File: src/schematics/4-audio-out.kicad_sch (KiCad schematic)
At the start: 7 parts

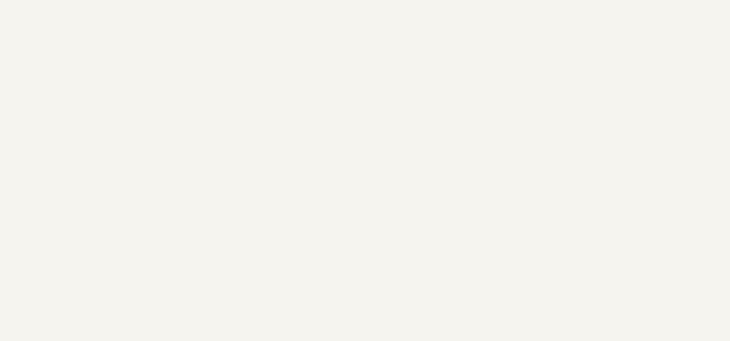
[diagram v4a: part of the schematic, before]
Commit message: Started to draw the MSF receiver based on the simulation learnings.
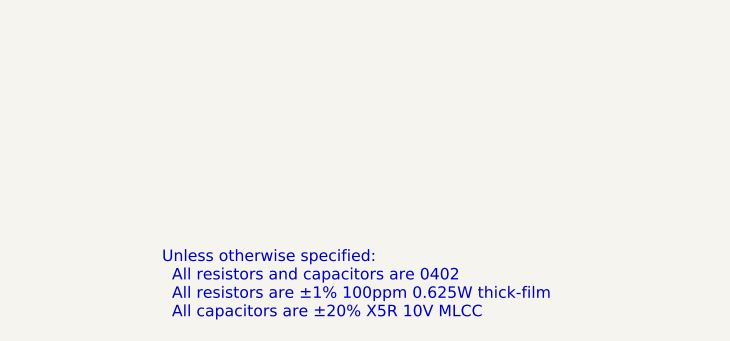
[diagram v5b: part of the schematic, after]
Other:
- note added: "Unless otherwise specified: All resistors and capacitors are 0402 All resistors are ±1% 100ppm 0.625W thick-film All capacitors are ±20% X5R 10V MLCC"
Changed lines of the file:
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@@
+    (effects (font (size 1.27 1.27)) (justify left bottom))
+  )
+  (text "Unless otherwise specified:\n  All resistors and capacitors are 0402\n  All resistors are ±1% 100ppm 0.625W thick-film\n  All capacitors are ±20% X5R 10V MLCC "
+    (at 301.244 261.62 0)
     (effects (font (size 1.27 1.27)) (justify left bottom))
   )

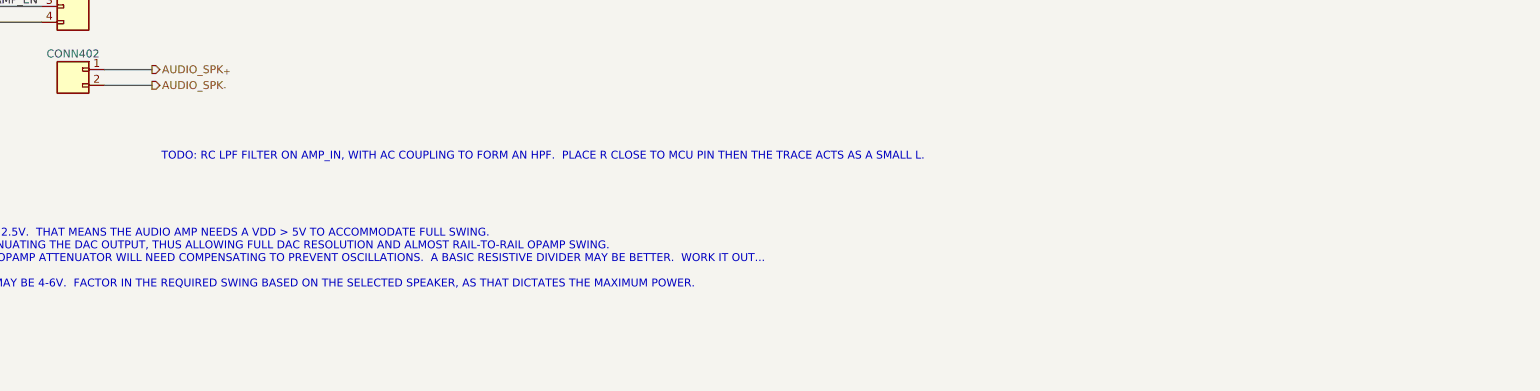
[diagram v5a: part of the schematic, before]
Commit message: Further elaboration of the MSF front-end.
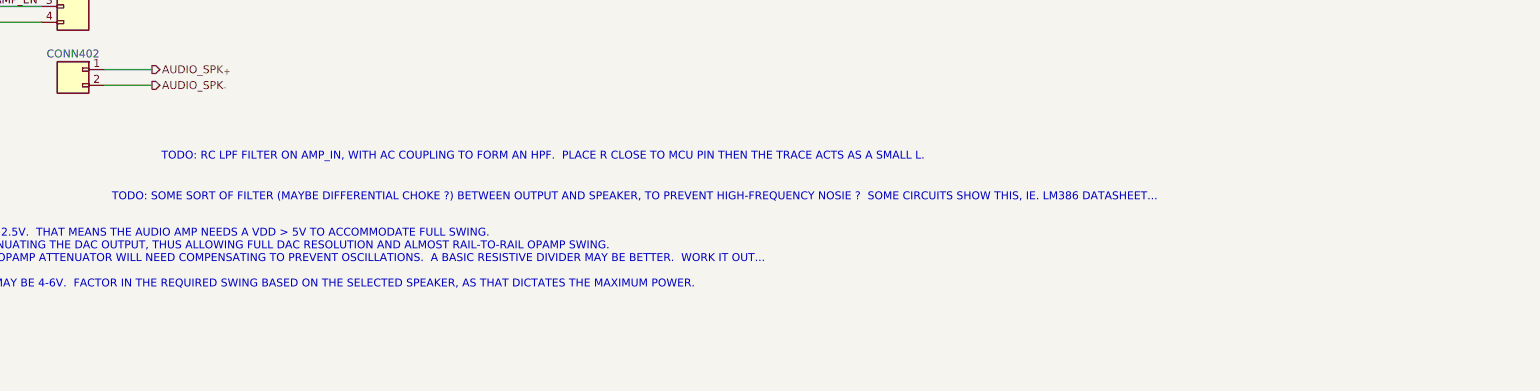
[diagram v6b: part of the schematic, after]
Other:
- note added: "TODO: SOME SORT OF FILTER (MAYBE DIFFERENTIAL CHOKE ?) BETWEEN OUTPUT AND SPEAKER, TO PREVENT HIGH-FREQUENCY NOSIE ? SOME CIRCUITS SHOW THIS, IE. LM386 DATASHEET..."
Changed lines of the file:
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@@
+    (effects (font (size 1.27 1.27)) (justify left bottom))
+  )
+  (text "TODO: SOME SORT OF FILTER (MAYBE DIFFERENTIAL CHOKE ?) BETWEEN OUTPUT AND SPEAKER, TO PREVENT HIGH-FREQUENCY NOSIE ?  SOME CIRCUITS SHOW THIS, IE. LM386 DATASHEET..."
+    (at 107.8471 96.2072 0)
     (effects (font (size 1.27 1.27)) (justify left bottom))
   )

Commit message: Started to elaborate the audio output circuitry.
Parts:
- removed C67: 4.7μF, restall-generic-capacitors:unpolarised-nominal-0402-1005, symbol restall-generic-capacitors:capacitor-unpolarised
- removed CONN401: header-1x4, symbol restall-generic-connectors:header-1x4
- removed CONN402: header-1x2, symbol restall-generic-connectors:header-1x2
- added C24, C25: 4.7μF, restall-generic-capacitors:unpolarised-nominal-0402-1005, symbol restall-generic-capacitors:capacitor-unpolarised
- added C26: 100nF, restall-generic-capacitors:unpolarised-nominal-1206-3216, symbol restall-generic-capacitors:capacitor-unpolarised
- added C27: DNP, restall-generic-capacitors:unpolarised-nominal-0402-1005, symbol restall-generic-capacitors:capacitor-unpolarised
- added R22: 33kΩ, restall-generic-resistors:nominal-0402-1005, symbol restall-generic-resistors:resistor
- added R23, R24: 19.6kΩ, restall-generic-resistors:nominal-0402-1005, symbol restall-generic-resistors:resistor
- added U2: IS31AP4991A-SLS2, restall-generic-sop:MSOP8-3x3mm-0.65mm, symbol restall-manufacturer-lumissil:IS31AP4991A-?LS2
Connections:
- net AMP_EN: now also R22.1, U2.1 (SDB)
- net AMP_IN: now also C26.1
- net AUDIO_AMP_{+5V}: now also FB3.1 (P1)
- net AUDIO_SPK_{+}: now also U2.8 (V_{O+})
- net AUDIO_SPK_{-}: now also C27.2, R24.2, U2.5 (V_{O-})
- net GND: now also C24.2, C25.2, R22.2, U2.7 (GND)
- net AUDIO_VDD_{+5V}: now reaches C64.1, C65.1, C66.1
- net AUDIO_VDD_{+5V}: now also FB3.2 (P2), C24.1, U2.6 (V_{CC})
- new net: C25.1, U2.2 (BYP), U2.3 (+)
- new net: C27.1, R23.2, R24.1, U2.4 (-)
- new net: C26.2, R23.1
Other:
- note added: "TODO: 4V_{pp} INTO 8 OHMS GIVES 1W; DAC OUTPUT IS 2.5V_{pp} SO AMPLIFICATION OF 1.6V/V IS REQUIRED FOR A 1W SPEAKER, ABOUT 354mA."
- note added: "TODO: DAC RECONSTRUCTION FILTER WILL BE NECESSARY (768kHz sample rate - 16-bit dithered; first alias (for 20kHz) is 748kHz). CAN EVEN BUILD THE GAIN INTO IT SO THAT THE POWER AMPLIFIER CAN USE 2x 19.6k RESISTORS EXPERIMENT WITH THE RESPONSE OF THIS FILTER (SPICE) - SEE IF THE 220pF CAP COULD BE REPLACED WITH (POSSIBLY) MORE ECONOMICAL AS 470pF+470pF BUT SIMILAR RESPONSE"
- note added: "TODO: PLACE R OF FILTER CLOSE TO MCU PIN THEN THE TRACE ACTS AS A SMALL L."
- note added: "TODO: SOME SORT OF FILTER (MAYBE DIFFERENTIAL CHOKE ?) BETWEEN OUTPUT AND SPEAKER, TO PREVENT HIGH-FREQUENCY NOISE ? SOME CIRCUITS SHOW THIS, IE. LM386 DATASHEET..."
- note added: "TODO: WHAT HARDWARE PROTECTIONS ARE THERE FOR THE SPEAKER ? FOR EXAMPLE, IF FIRMWARE SELECTS 3.3V REF OR THE INPUT CAP FAILS SHORT AND OPAMP PEGS TO THE RAILS AND THE SPEAKER SUDDENLY GETS 6V BETWEEN ITS TERMINALS ? MASSIVE DC-BLOCKING CAP WOULD BE REQUIRED (>= 100uF FOR 8-OHM SPEAKER); LEAVING IT OUT COULD CREATE A DC VOLTAGE ACROSS THE SPEAKER, WHICH COULD OVERHEAT. A 5W OR GREATER 8-OHM SPEAKE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"
- note removed: "TODO: AUDIO +5V OUT"
- note removed: "TODO: DAC OUTPUT IS 2.5V. THAT MEANS THE AUDIO AMP NEEDS A VDD > 5V TO ACCOMMODATE FULL SWING. REMEDY THIS BY ATTENUATING THE DAC OUTPUT, THUS ALLOWING FULL DAC RESOLUTION AND ALMOST RAIL-TO-RAIL OPAMP SWING. CAUTION - INVERTING OPAMP ATTENUATOR WILL NEED COMPENSATING TO PREVENT OSCILLATIONS. A BASIC RESISTIVE DIVIDER MAY BE BETTER. WORK IT OUT... ALSO, THE USB VBUS MAY BE 4-6V. FACTOR IN THE REQ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"
- note removed: "TODO: RC LPF FILTER ON AMP_IN, WITH AC COUPLING TO FORM AN HPF. PLACE R CLOSE TO MCU PIN THEN THE TRACE ACTS AS A SMALL L."
- note removed: "TODO: SOME SORT OF FILTER (MAYBE DIFFERENTIAL CHOKE ?) BETWEEN OUTPUT AND SPEAKER, TO PREVENT HIGH-FREQUENCY NOSIE ? SOME CIRCUITS SHOW THIS, IE. LM386 DATASHEET..."
- moved on the sheet: FB3

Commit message: Started drawing up the audio output schematic.  Added a simulation to verify the DAC reconstruction filter.
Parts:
- added C31: 100nF, restall-generic-capacitors:unpolarised-nominal-1206-3216, symbol restall-generic-capacitors:capacitor-unpolarised
- added C32, C33: 4.7nF, restall-generic-capacitors:unpolarised-nominal-0603-1608, symbol restall-generic-capacitors:capacitor-unpolarised
- added C34: 22pF, restall-generic-capacitors:unpolarised-nominal-0402-1005, symbol restall-generic-capacitors:capacitor-unpolarised
- added C35, C36: 4.7μF, restall-generic-capacitors:unpolarised-nominal-0402-1005, symbol restall-generic-capacitors:capacitor-unpolarised
- added D8: SD103AWS, restall-generic-sot:SOD-323, symbol restall-generic-diodes:schottky
- added R25: 68kΩ, restall-generic-resistors:nominal-0402-1005, symbol restall-generic-resistors:resistor
- added R29: 19.6kΩ, restall-generic-resistors:nominal-0402-1005, symbol restall-generic-resistors:resistor
- added R30: 5.1kΩ, restall-generic-resistors:nominal-0402-1005, symbol restall-generic-resistors:resistor
- added R31: 16kΩ, restall-generic-resistors:nominal-0402-1005, symbol restall-generic-resistors:resistor
- added R32: 39kΩ, restall-generic-resistors:nominal-0402-1005, symbol restall-generic-resistors:resistor
- added U4: MCP6486U, restall-generic-sot:SOT353, symbol restall-manufacturer-microchip:MCP6486U?-?-?T
- added U5: AP22653AW6, restall-manufacturer-diodes-inc:SOT26, symbol restall-manufacturer-diodes-inc:AP22653?W6
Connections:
- net AMP_IN: now also C31.1; no longer C26.1
- net AUDIO_AMP_{+5V}: now also U5.1 (IN); no longer FB3.1 (P1)
- net AUDIO_VDD_{+5V}: now also C35.1, D8.1 (K), U4.5 (V_{DD})
- net GND: now also C32.1, C33.1, C35.2, C36.2, R25.2, U4.2 (V_{SS}), U5.2 (GND)
- net at C25.1, U2.2 (BYP), U2.3 (+): now also C36.1, D8.2 (A), U4.1 (+)
- new net: C34.1, R31.2, U4.3 (-)
- new net: C26.1, C34.2, R32.2, U4.4
- new net: C31.2, R29.1
- new net: R25.1, U5.5 (ILIMIT)
- new net: C32.2, R29.2, R30.1
- new net: FB3.1 (P1), U5.6 (OUT)
- new net: C33.2, R30.2, R31.1, R32.1
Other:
- note added: "124≤f_{-3dB}≤20.7kHz Nominal -100dB@748kHz (alias of 20kHz)"
- note added: "309mA≤I_{max}≤402mA"
- note added: "3^{rd} Order MFB with Chebyshev Response and Nominal 1.6V/V Gain"
- note added: "Current limiting to reduce the probability of an 8Ω±15% speaker being damaged if more than 1.5W is dissipated due to a fault, such as the op-amp pegging to the rails and putting DC across it. The latch-on-fault 'A' variant ensures current is removed and not merely limited in the event of a fault. The tolerances of the speaker and current limiter are such that loud sounds could also cause trips, b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"
- note added: "Differential Power Amplifier (1W Nominal)"
- note added: "Nominal 0-2.5V 768kSps (dithered 48kSps)"
- note added: "Nominal ±4V_{max} 304mA_{rms}≤I_{max}≤397mA_{rms}"
- note added: "TODO: BYPASS CAPS FOR INPUT AND OUTPUT OF AP22653AW6"
- note added: "TODO: WHAT TO DO WITH ~{FAULT} ? WOULD BE NICE TO TIE TO THE 'EN' PIN AS OPEN-DRAIN BUT THAT WILL PROBABLY OSCILLATE"
- note removed: "TODO: 4V_{pp} INTO 8 OHMS GIVES 1W; DAC OUTPUT IS 2.5V_{pp} SO AMPLIFICATION OF 1.6V/V IS REQUIRED FOR A 1W SPEAKER, ABOUT 354mA."
- note removed: "TODO: DAC RECONSTRUCTION FILTER WILL BE NECESSARY (768kHz sample rate - 16-bit dithered; first alias (for 20kHz) is 748kHz). CAN EVEN BUILD THE GAIN INTO IT SO THAT THE POWER AMPLIFIER CAN USE 2x 19.6k RESISTORS EXPERIMENT WITH THE RESPONSE OF THIS FILTER (SPICE) - SEE IF THE 220pF CAP COULD BE REPLACED WITH (POSSIBLY) MORE ECONOMICAL AS 470pF+470pF BUT SIMILAR RESPONSE"
- note removed: "TODO: PLACE R OF FILTER CLOSE TO MCU PIN THEN THE TRACE ACTS AS A SMALL L."
- note removed: "TODO: SOME SORT OF FILTER (MAYBE DIFFERENTIAL CHOKE ?) BETWEEN OUTPUT AND SPEAKER, TO PREVENT HIGH-FREQUENCY NOISE ? SOME CIRCUITS SHOW THIS, IE. LM386 DATASHEET..."
- note removed: "TODO: WHAT HARDWARE PROTECTIONS ARE THERE FOR THE SPEAKER ? FOR EXAMPLE, IF FIRMWARE SELECTS 3.3V REF OR THE INPUT CAP FAILS SHORT AND OPAMP PEGS TO THE RAILS AND THE SPEAKER SUDDENLY GETS 6V BETWEEN ITS TERMINALS ? MASSIVE DC-BLOCKING CAP WOULD BE REQUIRED (>= 100uF FOR 8-OHM SPEAKER); LEAVING IT OUT COULD CREATE A DC VOLTAGE ACROSS THE SPEAKER, WHICH COULD OVERHEAT. A 5W OR GREATER 8-OHM SPEAKE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"
- moved on the sheet: C24, C25, C26, C27, C64, C65, C66, FB3, R22, R23, R24, U2A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
